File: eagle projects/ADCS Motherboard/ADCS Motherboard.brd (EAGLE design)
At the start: 91 x 91 mm, 145 parts, among them J1 HDR_10_EZFET_DEBUGGER, J2A 832-10-012-10-005000, J2B 832-10-012-10-005000, J3 832-10-012-10-005000, J5 CNC_3221-10-0300-00, J7 TE-1734829-3, J8 830-10-006-20-005000, Q1 BSR802NL6327HTSA1, U1 MSP430F5529IPN, U10 TSV991AILT, U2 TSV991AILT, U3 ADS7841E_2K5, U4 TSV991AILT, U5 DMC4050SSDQ-13, U6 BNO055, U7 HMC1053, U9 BMX160, Y1 32.768kHz, Y2 CSTCR4M00G15L99, Y3 32.768kHz

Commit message: Updated footprint names
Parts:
- renumbered J2A to JP2A, J2B to JP2B

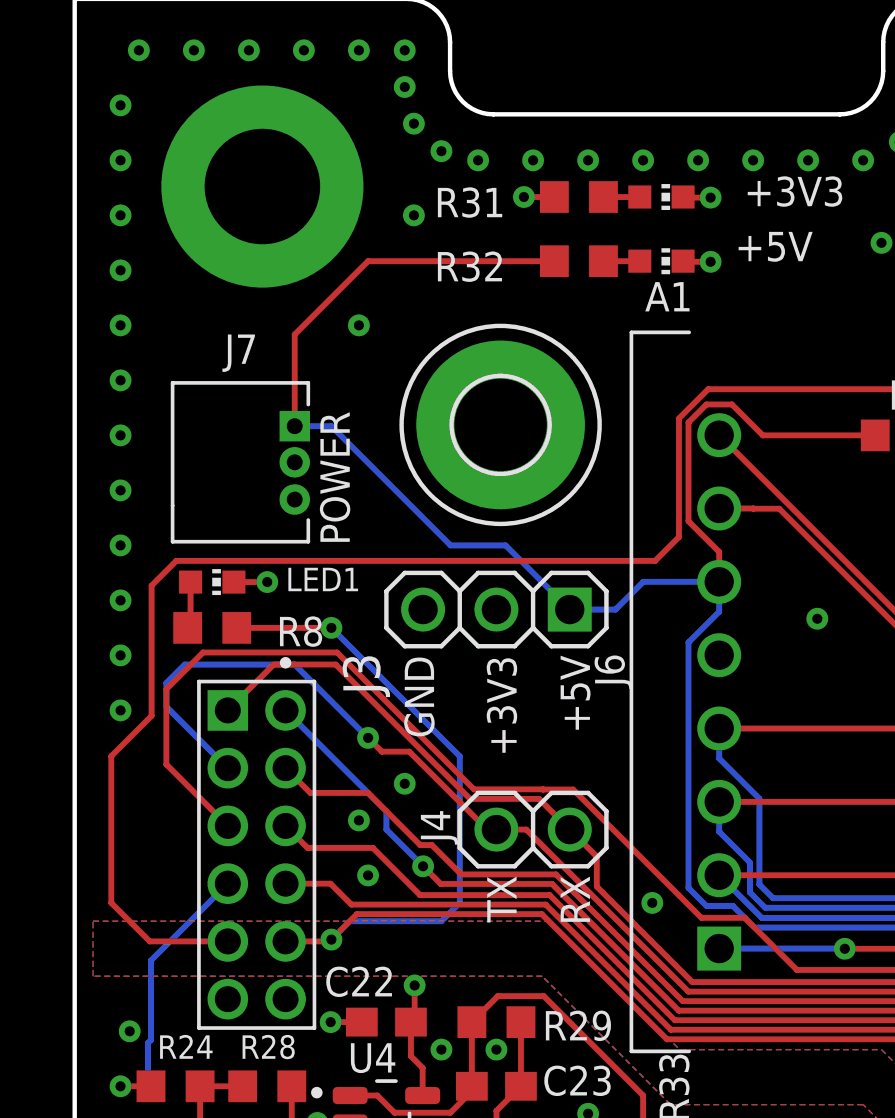
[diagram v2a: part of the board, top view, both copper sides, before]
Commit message: Removed LEDs from MOBO
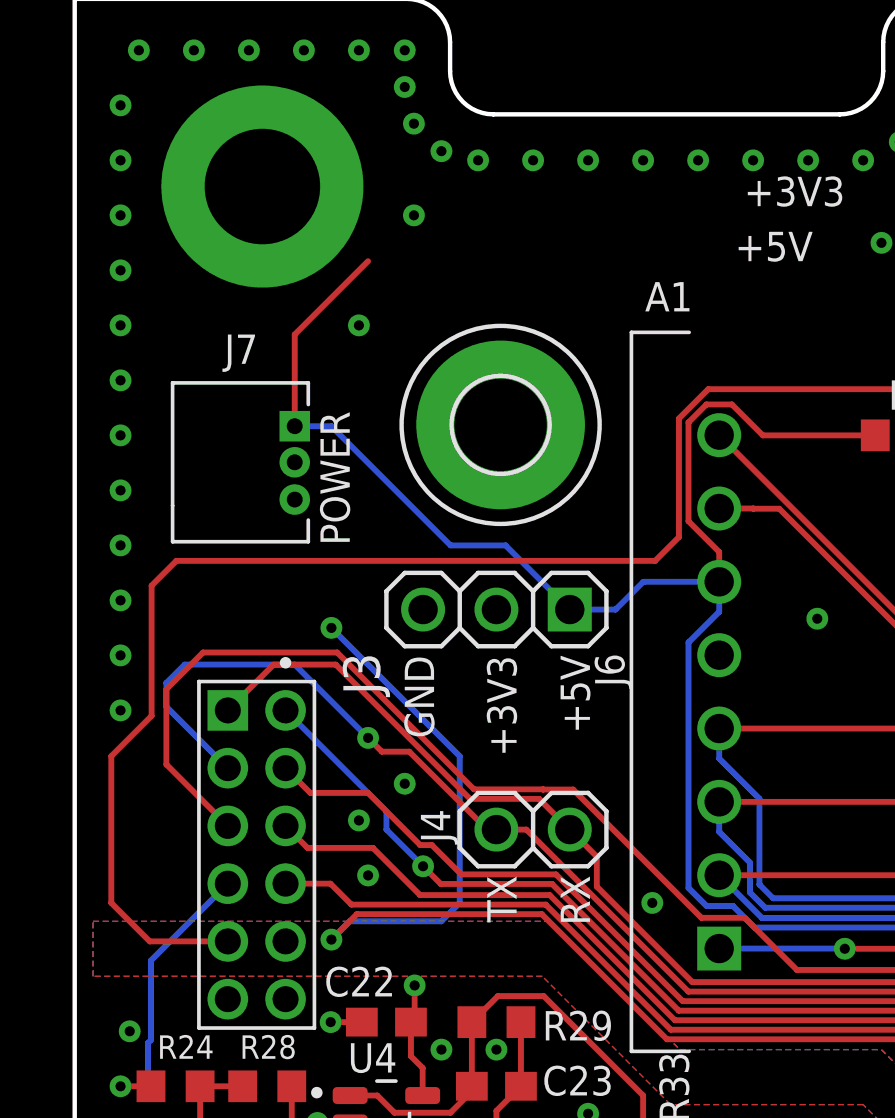
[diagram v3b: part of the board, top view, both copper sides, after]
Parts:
- removed LED1, LED2, LED3: (no value), led:CHIP-LED0603
- removed R31, R8: 470R, rcl:R0603
- removed R32: 750R, rcl:R0603
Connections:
- removed net N$4: LED1.A, R8.2
- removed net N$5: LED2.A, R31.2
- removed net N$6: LED3.A, R32.2
- net +3V3: no longer R31.1
- net +5V: no longer R32.1
- net GND: no longer LED1.C, LED2.C, LED3.C
- net MSP430_ACTIVE: no longer J3.10, R8.1
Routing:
- net +5V: track 105.6 -> 99.1 mm
- net MSP430_ACTIVE: track 96.8 -> 92.0 mm
- net GND: track 83.5 -> 80.4 mm, vias 316 -> 313
- net N$4: track 1.69 -> 0.00 mm
- net N$6: track 1.26 -> 0.00 mm
- net N$5: track 1.26 -> 0.00 mm
- net +3V3: track 84.8 -> 83.6 mm, vias 25 -> 24

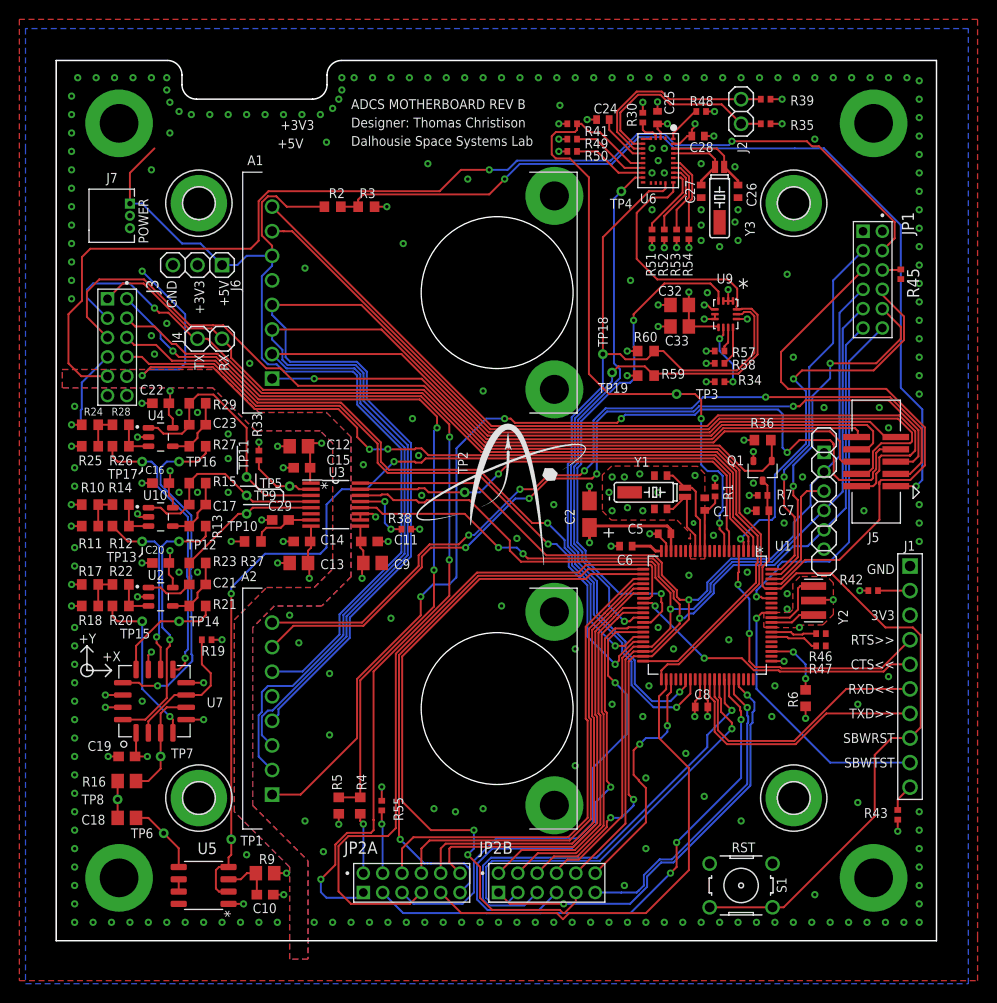
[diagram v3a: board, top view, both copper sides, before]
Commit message: Air wires and wire stubs fixed on all boards
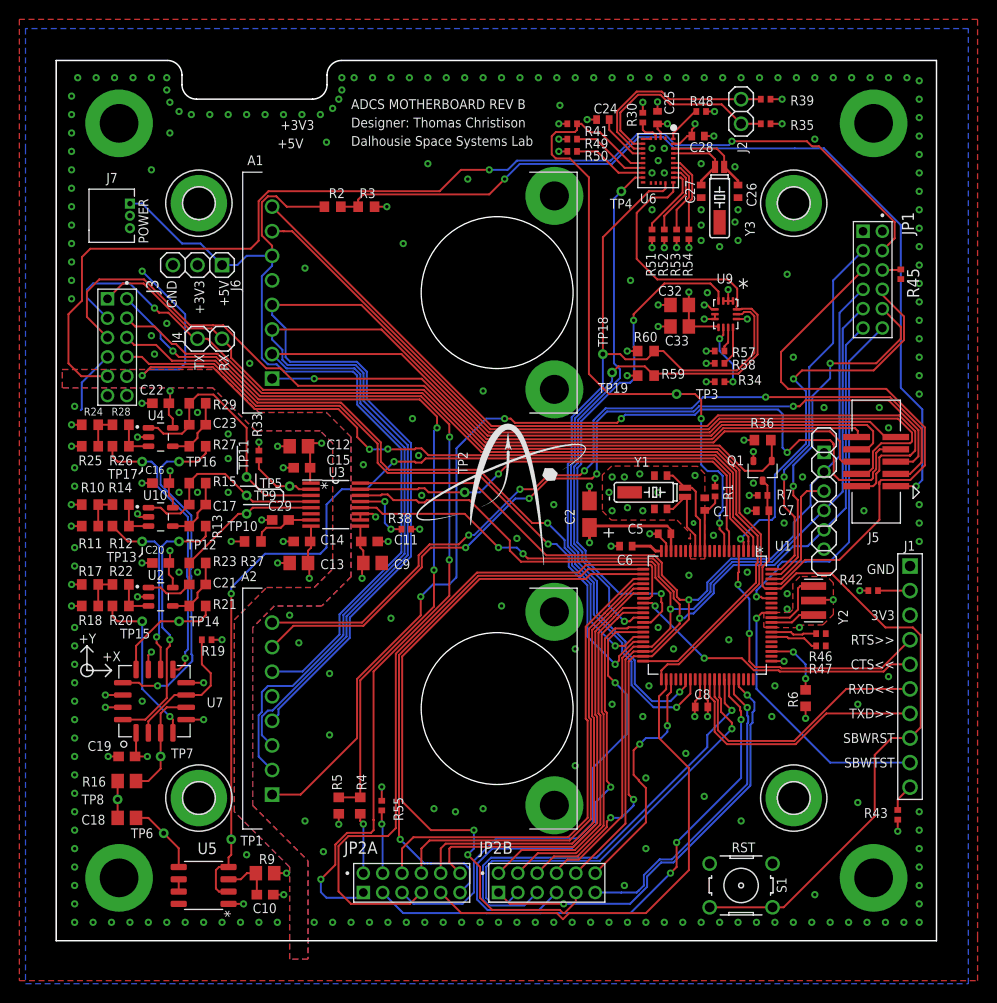
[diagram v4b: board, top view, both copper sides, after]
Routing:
- net +5V: track 99.1 -> 92.4 mm
- net +3V3: track 83.6 -> 81.8 mm
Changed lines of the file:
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@@
 <wire x1="19.6925" y1="70.81" x2="18.7325" y2="69.85" width="0.2032" layer="16"/>
 <wire x1="18.7325" y1="69.85" x2="17.145" y2="69.85" width="0.2032" layer="16"/>
-<wire x1="7.62" y1="76.2" x2="7.62" y2="79.375" width="0.2032" layer="1"/>
-<wire x1="7.62" y1="79.375" x2="10.16" y2="81.915" width="0.2032" layer="1"/>
 <wire x1="14.9225" y1="72.0725" x2="17.145" y2="69.85" width="0.2032" layer="16"/>
 <wire x1="13.0175" y1="72.0725" x2="14.9225" y2="72.0725" width="0.2032" layer="16"/>
@@
 <contactref element="R7" pad="2"/>
 <wire x1="63.56" y1="42.0555" x2="63.5404" y2="42.0751" width="0.3048" layer="1"/>
-<wire x1="67.3631" y1="24.1681" x2="67.3131" y2="24.13" width="0.254" layer="1"/>
-<wire x1="67.3131" y1="24.13" x2="67.3608" y2="24.13" width="0.254" layer="1"/>
-<wire x1="63.56" y1="42.0555" x2="63.56" y2="42.2564" width="0.254" layer="1"/>
 <wire x1="63.56" y1="42.0055" x2="63.5404" y2="42.0751" width="0.3048" layer="1"/>
 <wire x1="63.56" y1="42.0055" x2="63.56" y2="40.285" width="0.254" layer="1"/>
@@
 <wire x1="11.7731" y1="56.8325" x2="11.7731" y2="55.6906" width="0.2032" layer="1"/>
 <wire x1="11.7731" y1="55.6906" x2="11.645" y2="55.5625" width="0.2032" layer="1"/>
-<wire x1="67.3631" y1="24.844" x2="67.3631" y2="24.1681" width="0.2032" layer="1"/>
 <wire x1="31.535" y1="41.275" x2="31.4452" y2="41.3648" width="0.2032" layer="1"/>
 <wire x1="31.4452" y1="41.3648" x2="31.4452" y2="42.8625" width="0.2032" layer="1"/>
@@
 <wire x1="11.7602" y1="39.1677" x2="11.645" y2="39.0525" width="0.2032" layer="1"/>
 <wire x1="11.645" y1="39.0525" x2="11.705" y2="38.9925" width="0.2032" layer="1"/>
-<wire x1="63.5404" y1="42.5046" x2="63.5404" y2="42.0751" width="0.3048" layer="1"/>
-<wire x1="63.5404" y1="42.5046" x2="63.1675" y2="42.8775" width="0.3048" layer="1"/>
-<wire x1="63.1675" y1="42.8775" x2="55.2888" y2="42.8775" width="0.3048" layer="1"/>
-<wire x1="67.3354" y1="23.1775" x2="67.3354" y2="24.1077" width="0.2032" layer="1"/>
-<wire x1="67.3354" y1="24.1077" x2="67.3131" y2="24.13" width="0.2032" layer="1"/>
+<wire x1="55.2888" y1="42.8775" x2="63.1675" y2="42.8775" width="0.3048" layer="1"/>
 <wire x1="26.0325" y1="39.0525" x2="26.0325" y2="40.32" width="0.2032" layer="1"/>
 <wire x1="26.0325" y1="40.32" x2="26.3525" y2="40.64" width="0.2032" layer="1"/>
@@
 <contactref element="J3" pad="7"/>
 <wire x1="2.6388" y1="54.94105" x2="2.54" y2="54.84225" width="0.2032" layer="16"/>
-<wire x1="2.54" y1="54.84225" x2="2.54" y2="53.34" width="0.2032" layer="16"/>
 <wire x1="5.3025" y1="60.3575" x2="2.6388" y2="57.6938" width="0.2032" layer="16"/>
 <wire x1="2.6388" y1="57.6938" x2="2.6388" y2="54.94105" width="0.2032" layer="16"/>
 <contactref element="J8" pad="6"/>
+<wire x1="67.3631" y1="24.844" x2="67.3631" y2="24.1681" width="0.2032" layer="1"/>
+<wire x1="67.3631" y1="24.1681" x2="67.3631" y2="23.2052" width="0.2032" layer="1"/>
+<wire x1="67.3631" y1="23.2052" x2="67.3354" y2="23.1775" width="0.2032" layer="1"/>
+<wire x1="63.1675" y1="42.8775" x2="63.56" y2="42.485" width="0.2032" layer="1"/>
+<wire x1="63.56" y1="42.485" x2="63.56" y2="42.0555" width="0.2032" layer="1"/>
 </signal>
 <signal name="GND">
@@
 <wire x1="13.335" y1="64.77" x2="8.89" y2="69.215" width="0.2032" layer="16"/>
 <via x="8.89" y="69.215" extent="1-16" drill="0.35"/>
-<wire x1="8.8275" y1="58.3575" x2="8.89" y2="58.42" width="0.2032" layer="1"/>
 <via x="8.89" y="58.42" extent="1-16" drill="0.35"/>
 <wire x1="8.89" y1="58.42" x2="9.525" y2="59.055" width="0.2032" layer="16"/>
 <wire x1="9.525" y1="59.055" x2="12.7" y2="59.055" width="0.2032" layer="16"/>
-<wire x1="9.77246875" y1="59.30246875" x2="8.89" y2="58.42" width="0.2032" layer="1"/>
-<wire x1="16.17583125" y1="59.30246875" x2="9.77246875" y2="59.30246875" width="0.2032" layer="1"/>
+<wire x1="9.77246875" y1="59.30246875" x2="16.17583125" y2="59.30246875" width="0.2032" layer="1"/>
+<wire x1="8.89" y1="58.42" x2="9.77246875" y2="59.30246875" width="0.2032" layer="1"/>
 </signal>
 <signal name="RESERVED_1">
